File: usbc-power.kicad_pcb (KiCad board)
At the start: 2 copper layers, 38.1 x 31.8 mm, 9 parts, among them J1 UJC-HP-3-SMT-TR, U1 NE555P

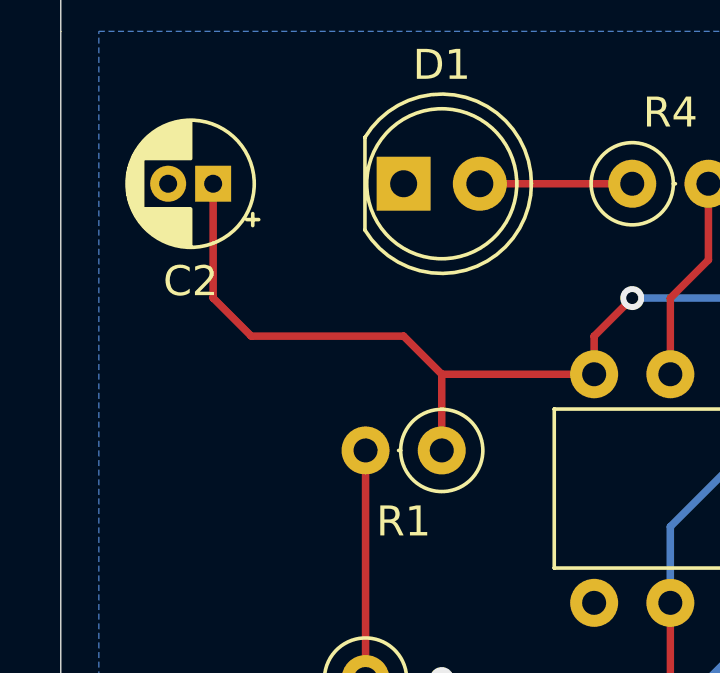
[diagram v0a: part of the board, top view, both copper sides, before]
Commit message: add current limiting resistor, generate gerbers
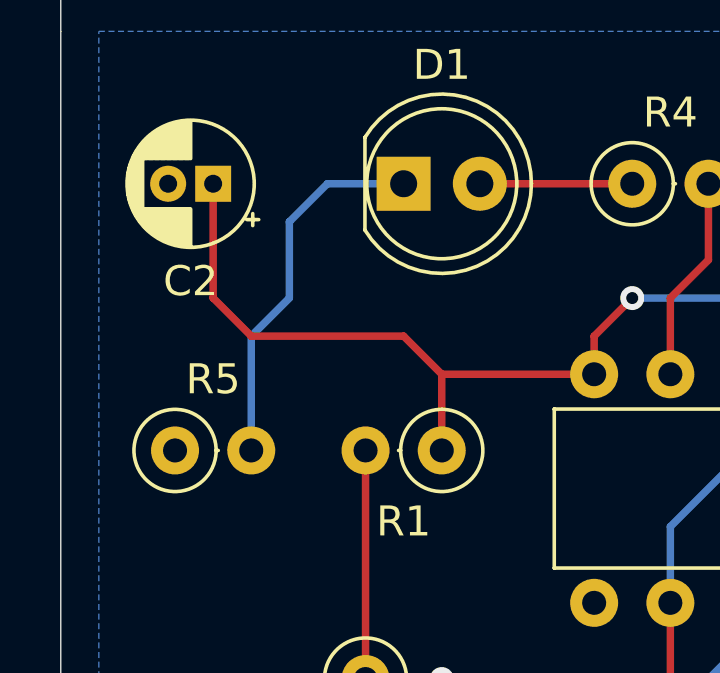
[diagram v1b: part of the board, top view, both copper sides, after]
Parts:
- added R5: R, Resistor_THT:R_Axial_DIN0207_L6.3mm_D2.5mm_P2.54mm_Vertical, F.Cu at (123.2, 83.8)
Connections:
- D1 pad 1: GND -> Net-(D1-Pad1)
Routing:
- net Net-(D1-Pad1): track 0.00 -> 12.5 mm
